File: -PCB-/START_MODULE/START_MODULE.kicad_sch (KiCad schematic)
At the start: 3 parts

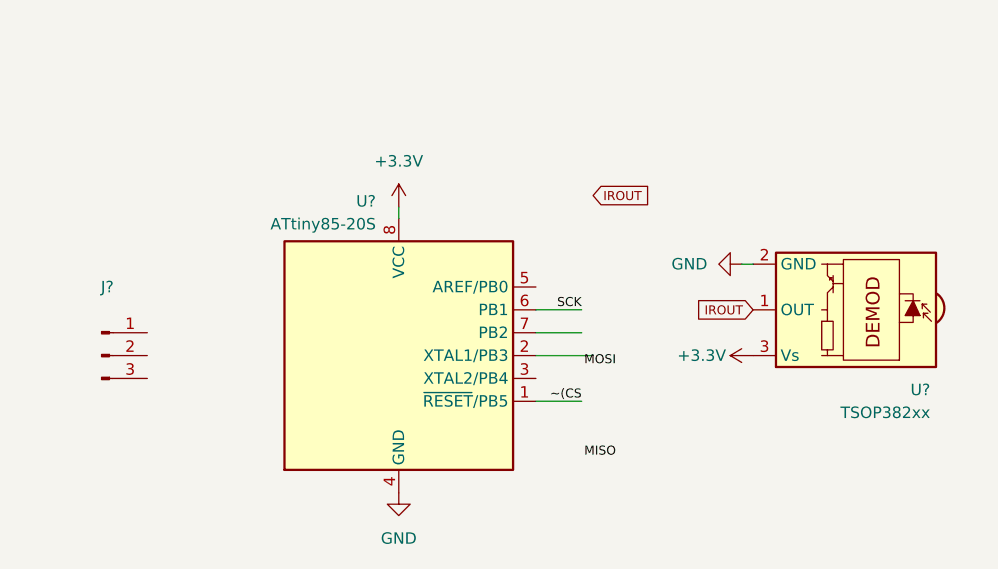
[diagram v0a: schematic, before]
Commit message: Start module PCB update
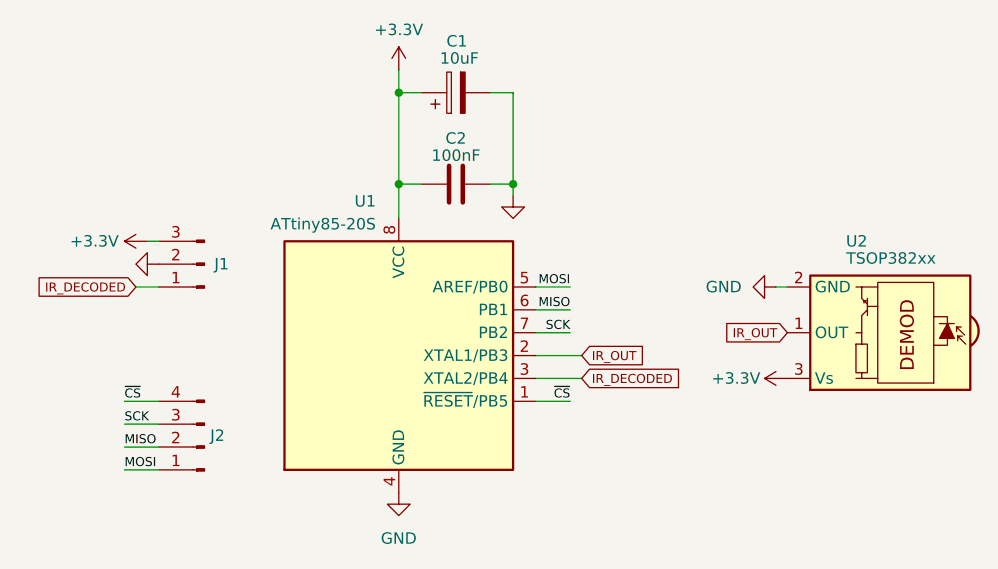
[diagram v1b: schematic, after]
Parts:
- added C1: 10uF, Capacitor_Tantalum_SMD:CP_EIA-3216-18_Kemet-A_Pad1.58x1.35mm_HandSolder, symbol Device:C_Polarized
- added C2: 100nF, Capacitor_SMD:C_0805_2012Metric_Pad1.18x1.45mm_HandSolder, symbol Device:C
- added J2: Conn_01x04_Pin, Connector_PinHeader_2.54mm:PinHeader_1x04_P2.54mm_Vertical, symbol Connector:Conn_01x04_Pin
- J1: renamed from J?; footprint (none) -> Connector_PinHeader_2.54mm:PinHeader_1x03_P2.54mm_Vertical
- gave numbers to parts that had none: 2
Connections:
- net IROUT is gone; now on net IR_OUT: U2.1 (OUT)
- net +3.3V: now also J1.3 (Pin_3), C1.1, C2.1
- net GND: now also J1.2 (Pin_2), C1.2, C2.2
- net MISO: now also U1.6 (PB1), J2.2 (Pin_2)
- net MOSI: now also U1.5 (AREF/PB0), J2.1 (Pin_1)
- net SCK: now also U1.7 (PB2), J2.3 (Pin_3); no longer U1.6 (PB1)
- net IR_DECODED: now reaches J1.1 (Pin_1)
- net IR_DECODED: now also U1.3 (XTAL2/PB4)
- net IR_OUT: now reaches U1.2 (XTAL1/PB3)
- net ~(CS renamed ~{CS}
- net ~{CS}: now also J2.4 (Pin_4)
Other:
- moved on the sheet: J1, U2

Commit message: Silkscreen update IR module
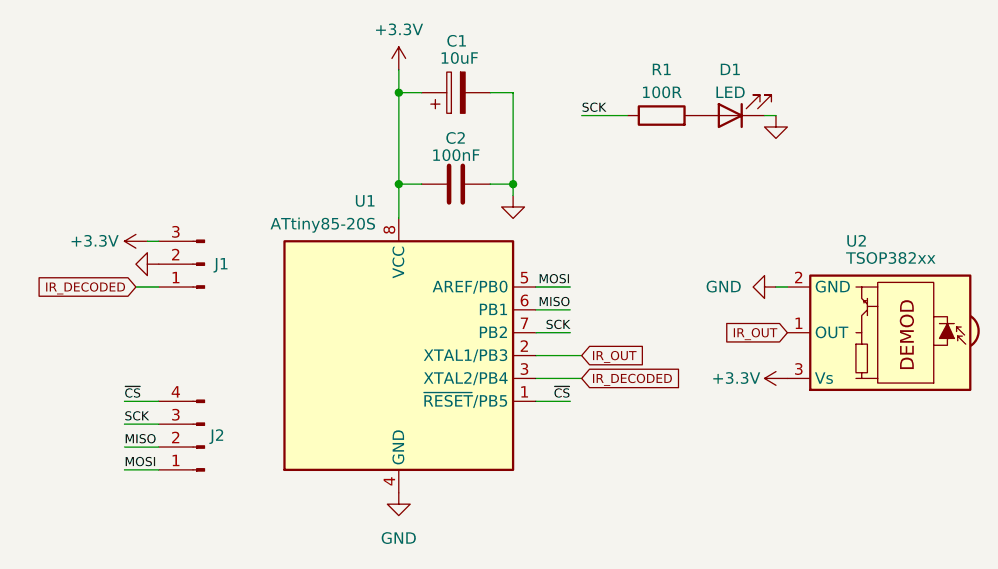
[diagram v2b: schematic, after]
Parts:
- added D1: LED, LED_SMD:LED_0805_2012Metric_Pad1.15x1.40mm_HandSolder, symbol Device:LED
- added R1: 100R, Resistor_SMD:R_0805_2012Metric_Pad1.20x1.40mm_HandSolder, symbol Device:R
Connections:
- net GND: now also D1.1 (K)
- net SCK: now also R1.1
- new net: D1.2 (A), R1.2
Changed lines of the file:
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@@
+	(wire
+		(pts
+			(xy 170.18 62.23) (xy 168.91 62.23)
+		)
+		(stroke
+			(width 0)
+			(type default)
+		)
+	)
 	(wire
 		(pts
@@
 		(pts
 			(xy 147.32 81.28) (xy 143.51 81.28)
+		)
+		(stroke
+			(width 0)
+			(type default)
+		)
+	)
+	(wire
+		(pts
+			(xy 148.59 62.23) (xy 153.67 62.23)
 		)
 		(stroke
@@
 		)
 	)
-	(label "~{CS}"
-		(at 147.32 93.98 180)
+	(label "SCK"
+		(at 148.59 62.23 0)
 		(fields_autoplaced yes)
 		(effects
@@
 				(color 0 0 0 1)
 			)
-			(justify right bottom)
-		)
-	)
-	(label "MOSI"
-		(at 97.79 101.6 0)
+			(justify left bottom)
+		)
+	)
+	(label "~{CS}"
+		(at 147.32 93.98 180)
 		(fields_autoplaced yes)
 		(effects
@@
 				(color 0 0 0 1)
 			)
-			(justify left bottom)
+			(justify right bottom)
 		)
 	)
 	(label "MOSI"
-		(at 147.32 81.28 180)
+		(at 97.79 101.6 0)
 		(fields_autoplaced yes)
 		(effects
@@
 				(color 0 0 0 1)
 			)
-			(justify right bottom)
-		)
-	)
-	(global_label "IR_DECODED"
-		(shape input)
-		(at 99.06 81.28 180)
+			(justify left bottom)
+		)
+	)
+	(label "MOSI"
+		(at 147.32 81.28 180)
 		(fields_autoplaced yes)
 		(effects
@@
 				(color 0 0 0 1)
 			)
-			(justify right)
-		)
-		(property "Intersheetrefs" "${INTERSHEET_REFS}"
-			(at 87.6144 81.28 0)
-			(effects
-				(font
-					(size 1.27 1.27)
-				)
-				(justify right)
-				(hide yes)
-			)
+			(justify right bottom)
 		)
 	)
 	(global_label "IR_DECODED"
 		(shape input)
-		(at 148.59 91.44 0)
+		(at 99.06 81.28 180)
 		(fields_autoplaced yes)
 		(effects
@@
 				(color 0 0 0 1)
 			)
-			(justify left)
+			(justify right)
 		)
 		(property "Intersheetrefs" "${INTERSHEET_REFS}"
-			(at 160.0356 91.44 0)
-			(effects
-				(font
-					(size 1.27 1.27)
-				)
-				(justify left)
-				(hide yes)
-			)
-		)
-	)
-	(global_label "IR_OUT"
+			(at 87.6144 81.28 0)
+			(effects
+				(font
+					(size 1.27 1.27)
+				)
+				(justify right)
+				(hide yes)
+			)
+		)
+	)
+	(global_label "IR_DECODED"
 		(shape input)
-		(at 171.45 86.36 180)
+		(at 148.59 91.44 0)
 		(fields_autoplaced yes)
 		(effects
@@
 				(color 0 0 0 1)
 			)
-			(justify right)
+			(justify left)
 		)
 		(property "Intersheetrefs" "${INTERSHEET_REFS}"
-			(at 164.0045 86.36 0)
-			(effects
-				(font
-					(size 1.27 1.27)
-				)
-				(justify right)
+			(at 160.0356 91.44 0)
+			(effects
+				(font
+					(size 1.27 1.27)
+				)
+				(justify left)
 				(hide yes)
 			)
@@
 	(global_label "IR_OUT"
 		(shape input)
-		(at 148.59 88.9 0)
+		(at 171.45 86.36 180)
 		(fields_autoplaced yes)
 		(effects
@@
 				(color 0 0 0 1)
 			)
+			(justify right)
+		)
+		(property "Intersheetrefs" "${INTERSHEET_REFS}"
+			(at 164.0045 86.36 0)
+			(effects
+				(font
+					(size 1.27 1.27)
+				)
+				(justify right)
+				(hide yes)
+			)
+		)
+	)
+	(global_label "IR_OUT"
+		(shape input)
+		(at 148.59 88.9 0)
+		(fields_autoplaced yes)
+		(effects
+			(font
+				(size 1 1)
+				(color 0 0 0 1)
+			)
 			(justify left)
 		)
@@
 		(dnp no)
 		(fields_autoplaced yes)
-		(property "Reference" "#PWR06"
+		(property "Reference" "#PWR07"
 			(at 163.83 81.28 0)
 			(effects
@@
 			(project "START_MODULE"
 				(path "/387968ee-398e-4575-a5f8-f6be4db04794"
-					(reference "#PWR06")
+					(reference "#PWR07")
 					(unit 1)
 				)
@@
 	)
 	(symbol
+		(lib_id "Device:R")
+		(at 157.48 62.23 90)
+		(unit 1)
+		(exclude_from_sim no)
+		(in_bom yes)
+		(on_board yes)
+		(dnp no)
+		(property "Reference" "R1"
+			(at 157.48 57.15 90)
+			(effects
+				(font
+					(size 1.27 1.27)
+				)
+			)
+		)
+		(property "Value" "100R"
+			(at 157.48 59.69 90)
+			(effects
+				(font
+					(size 1.27 1.27)
+				)
+			)
+		)
+		(property "Footprint" "Resistor_SMD:R_0805_2012Metric_Pad1.20x1.40mm_HandSolder"
+			(at 157.48 64.008 90)
+			(effects
+				(font
+					(size 1.27 1.27)
+				)
+				(hide yes)
+			)
+		)
+		(property "Datasheet" "~"
+			(at 157.48 62.23 0)
+			(effects
+				(font
+					(size 1.27 1.27)
+				)
+				(hide yes)
+			)
+		)
+		(property "Description" "Resistor"
+			(at 157.48 62.23 0)
+			(effects
+				(font
+					(size 1.27 1.27)
+				)
+				(hide yes)
+			)
+		)
+		(pin "1"
+		)
+		(pin "2"
+		)
+		(instances
+			(project ""
+				(path "/387968ee-398e-4575-a5f8-f6be4db04794"
+					(reference "R1")
+					(unit 1)
+				)
+			)
+		)
+	)
+	(symbol
 		(lib_id "Connector:Conn_01x03_Pin")
 		(at 106.68 78.74 180)
@@
 	)
 	(symbol
+		(lib_id "power:GND")
+		(at 170.18 62.23 0)
+		(unit 1)
+		(exclude_from_sim no)
+		(in_bom yes)
+		(on_board yes)
+		(dnp no)
+		(fields_autoplaced yes)
+		(property "Reference" "#PWR06"
+			(at 170.18 68.58 0)
+			(effects
+				(font
+					(size 1.27 1.27)
+				)
+				(hide yes)
+			)
+		)
+		(property "Value" "GND"
+			(at 170.18 67.31 0)
+			(effects
+				(font
+					(size 1.27 1.27)
+				)
+				(hide yes)
+			)
+		)
+		(property "Footprint" ""
+			(at 170.18 62.23 0)
+			(effects
+				(font
+					(size 1.27 1.27)
+				)
+				(hide yes)
+			)
+		)
+		(property "Datasheet" ""
+			(at 170.18 62.23 0)
+			(effects
+				(font
+					(size 1.27 1.27)
+				)
+				(hide yes)
+			)
+		)
+		(property "Description" "Power symbol creates a global label with name \"GND\" , ground"
+			(at 170.18 62.23 0)
+			(effects
+				(font
+					(size 1.27 1.27)
+				)
+				(hide yes)
+			)
+		)
+		(pin "1"
+		)
+		(instances
+			(project "START_MODULE"
+				(path "/387968ee-398e-4575-a5f8-f6be4db04794"
+					(reference "#PWR06")
+					(unit 1)
+				)
+			)
+		)
+	)
+	(symbol
 		(lib_id "power:+3.3V")
 		(at 100.33 76.2 90)
@@
 	)
 	(symbol
+		(lib_id "Device:LED")
+		(at 165.1 62.23 180)
+		(unit 1)
+		(exclude_from_sim no)
+		(in_bom yes)
+		(on_board yes)
+		(dnp no)
+		(property "Reference" "D1"
+			(at 165.1 57.15 0)
+			(effects
+				(font
+					(size 1.27 1.27)
+				)
+			)
+		)
+		(property "Value" "LED"
+			(at 165.1 59.69 0)
+			(effects
+				(font
+					(size 1.27 1.27)
+				)
+			)
+		)
+		(property "Footprint" "LED_SMD:LED_0805_2012Metric_Pad1.15x1.40mm_HandSolder"
+			(at 165.1 62.23 0)
+			(effects
+				(font
+					(size 1.27 1.27)
+				)
+				(hide yes)
+			)
+		)
+		(property "Datasheet" "~"
+			(at 165.1 62.23 0)
+			(effects
+				(font
+					(size 1.27 1.27)
+				)
+				(hide yes)
+			)
+		)
+		(property "Description" "Light emitting diode"
+			(at 165.1 62.23 0)
+			(effects
+				(font
+					(size 1.27 1.27)
+				)
+				(hide yes)
+			)
+		)
+		(pin "1"
+		)
+		(pin "2"
+		)
+		(instances
+			(project ""
+				(path "/387968ee-398e-4575-a5f8-f6be4db04794"
+					(reference "D1")
+					(unit 1)
+				)
+			)
+		)
+	)
+	(symbol
 		(lib_id "power:GND")
 		(at 101.6 78.74 270)
@@
 		(on_board yes)
 		(dnp no)
-		(property "Reference" "#PWR07"
+		(property "Reference" "#PWR08"
 			(at 175.26 91.44 0)
 			(effects
@@
 			(project "START_MODULE"
 				(path "/387968ee-398e-4575-a5f8-f6be4db04794"
-					(reference "#PWR07")
-					(unit 1)
-				)
+					(reference "#PWR08")
+					(unit 1)
+				)
